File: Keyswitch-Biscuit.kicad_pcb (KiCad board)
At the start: 2 copper layers, 18 x 18 mm, 7 parts, among them J1 Conn_01x03_Male, J2 Conn_01x03_Male, J3 Conn_01x03_Male, J4 Conn_01x03_Male

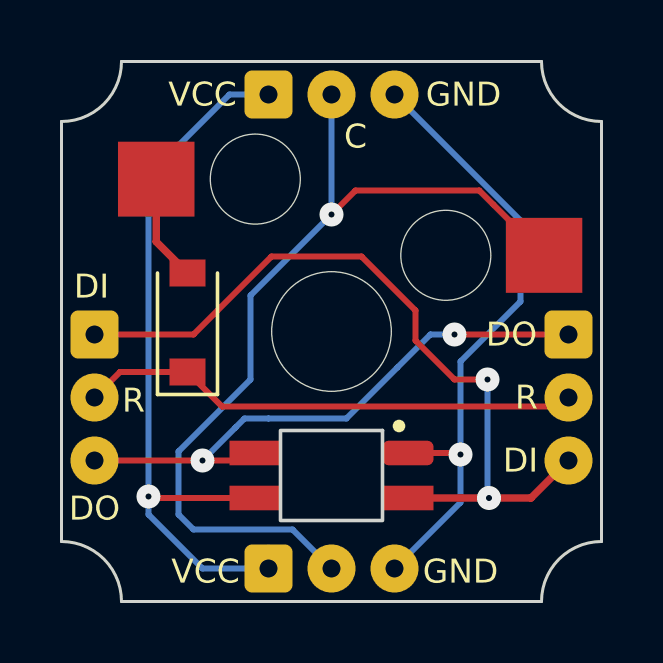
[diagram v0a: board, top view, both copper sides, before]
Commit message: Looked into tolerances and it turns out I should be okay making traces quite a lot smaller
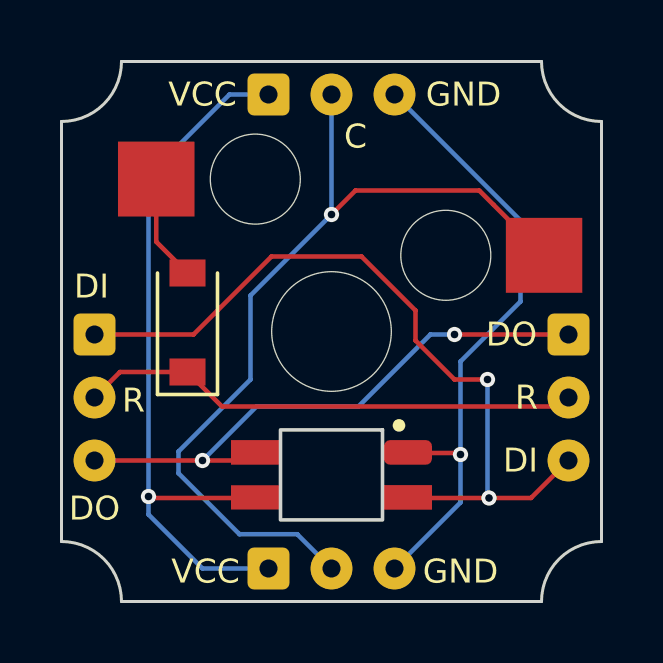
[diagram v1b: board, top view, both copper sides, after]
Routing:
- net Col: track 30.3 -> 29.5 mm
- net VCC: track 25.4 -> 24.7 mm
- net DataIn: track 26.9 -> 26.3 mm
